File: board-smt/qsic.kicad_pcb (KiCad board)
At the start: 4 copper layers, 214.1 x 131.7 mm, 177 parts, among them Q201 Dual_NMOS, Q202 Dual_NMOS, Q203 Dual_NMOS, Q204 Dual_NMOS, Q205 Dual_NMOS, Q206 Dual_NMOS, Q207 Dual_NMOS, Q208 Dual_NMOS, Q209 Dual_NMOS, Q210 Dual_NMOS, Q211 Dual_NMOS, Q212 Dual_NMOS, Q301 Dual_NMOS, Q302 Dual_NMOS, Q303 Dual_NMOS, Q304 Dual_NMOS, Q305 Dual_NMOS, Q306 Dual_NMOS, Q307 Dual_NMOS, U201 CMP401, U202 CMP401, U203 CMP401, U204 CMP401, U205 CMP401, U206 CMP401, U301 CMP401, U302 CMP401, U303 CMP401, U304 CMP401, U305 CMP401

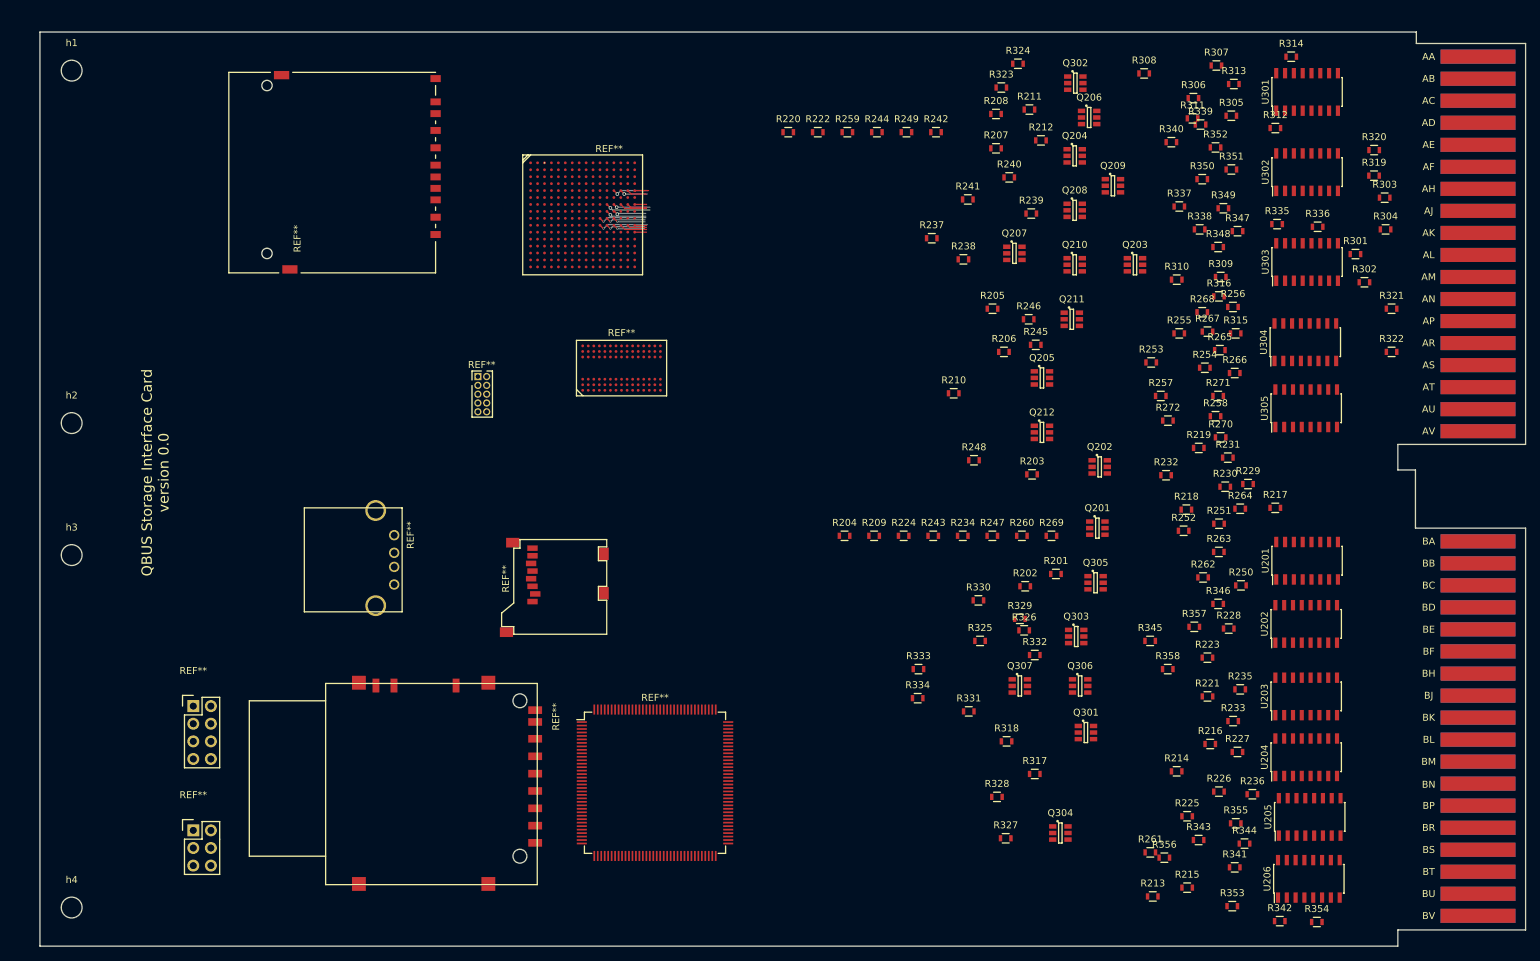
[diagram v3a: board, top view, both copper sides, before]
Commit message: Added the FPGA and rearranged the sheets.
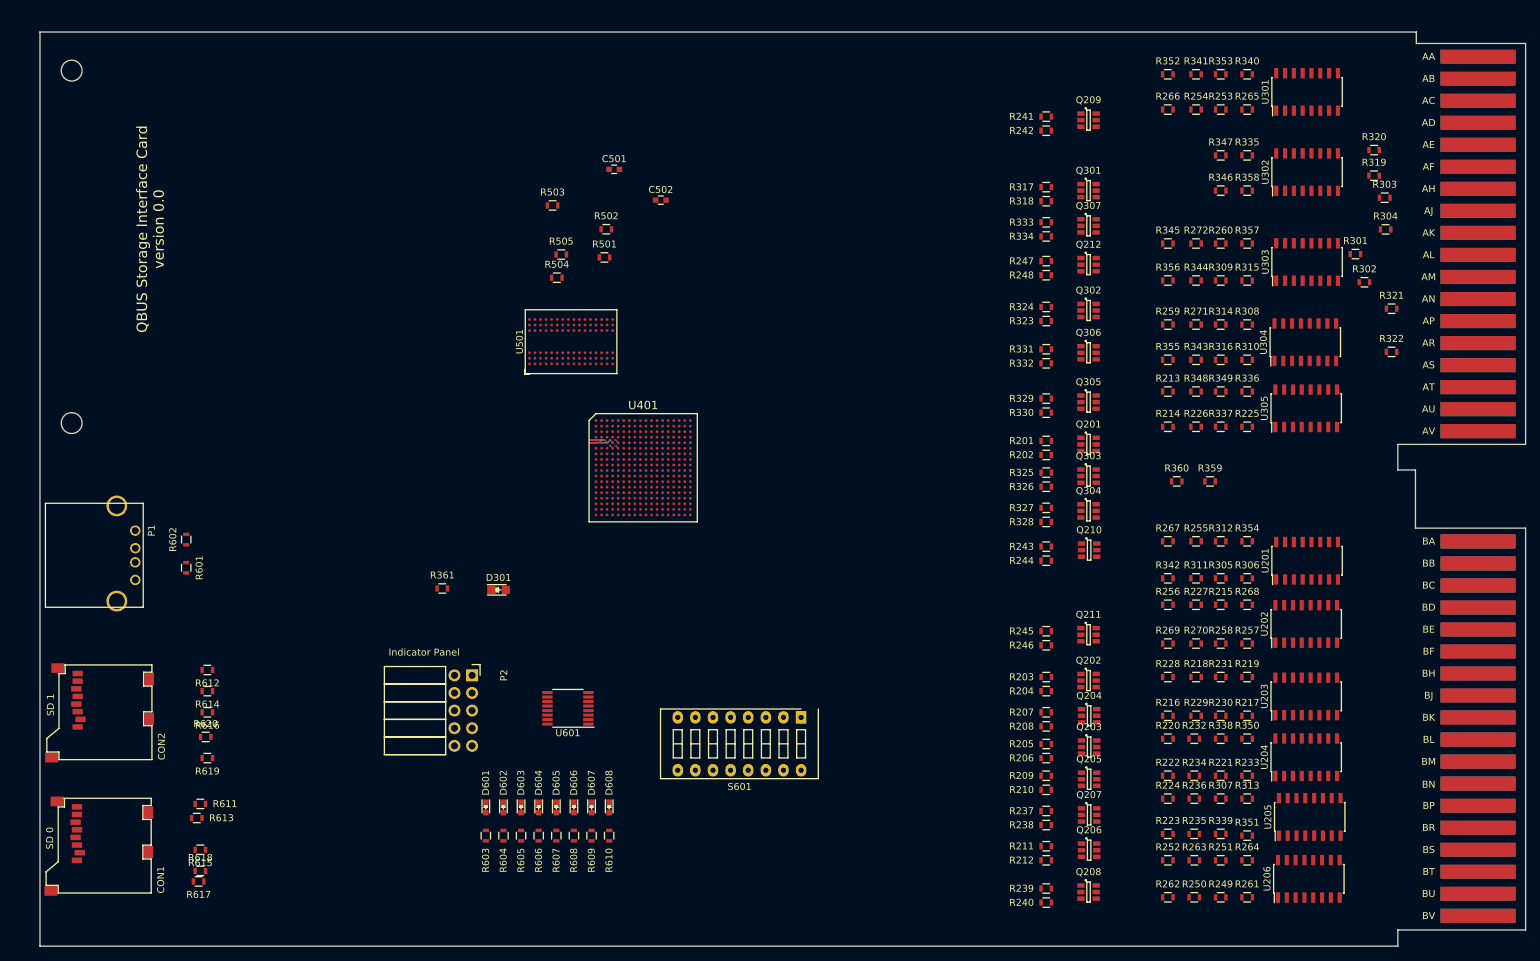
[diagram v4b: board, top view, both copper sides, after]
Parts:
- removed the REF** at (110.5, 51.8)
- removed the REF** at (101.3, 98.3)
- removed the REF** at (32.3, 126.1)
- removed the REF** at (116.1, 73.8)
- removed the REF** at (120.9, 133.6)
- removed the REF** at (83.3, 97.9)
- removed the REF** at (89.3, 45.2)
- removed the REF** at (54.4, 122.6)
- removed the REF** at (54.4, 140.5)
- removed the REF** at (95.4, 75.1)
- removed the REF** at (101.4, 121.8)
- removed h3, h4: MountingHole_3mm, Mounting_Holes:MountingHole_3mm
- added C501: 100nF, Capacitors_SMD:C_0603, F.Cu at (115.0, 45.2)
- added C502: 100nF, Capacitors_SMD:C_0603, F.Cu at (121.7, 49.6)
- added CON1: SD 0, myMods.pretty:microSD-3M-2900-series, F.Cu at (35.7, 135.6)
- added CON2: SD 1, microSD-3M-2900-series, F.Cu at (35.8, 116.4)
- added D301: LED_Small_ALT, LEDs:LED-0805, F.Cu at (98.4, 105.8)
- added D601: LED 0, LEDs:LED-0603, F.Cu at (96.5, 137.2)
- added D602: LED 1, LEDs:LED-0603, F.Cu at (99.1, 137.2)
- added D603: LED 2, LEDs:LED-0603, F.Cu at (101.6, 137.2)
- added D604: LED 3, LEDs:LED-0603, F.Cu at (104.1, 137.2)
- added D605: LED 4, LEDs:LED-0603, F.Cu at (106.7, 137.2)
- added D606: LED 5, LEDs:LED-0603, F.Cu at (109.2, 137.2)
- added D607: LED 6, LEDs:LED-0603, F.Cu at (111.8, 137.2)
- added D608: LED 7, LEDs:LED-0603, F.Cu at (114.3, 137.2)
- added P1: USB_A, Connect:USB_A, F.Cu at (46.0, 97.3)
- added P2: Indicator Panel, Socket_Strips:Socket_Strip_Angled_2x05, F.Cu at (94.5, 118.1)
- added R359: 5kΩ, Resistors_SMD:R_0603, F.Cu at (200.9, 90.2)
- added R360: 5kΩ, Resistors_SMD:R_0603, F.Cu at (196.1, 90.2)
- added R361: 240, Resistors_SMD:R_0603, F.Cu at (90.2, 105.6)
- added R501: 47k, Resistors_SMD:R_0603, F.Cu at (113.6, 57.9)
- added R502: 89, Resistors_SMD:R_0603, F.Cu at (113.9, 53.8)
- added R503: 47, Resistors_SMD:R_0603, F.Cu at (106.1, 50.4)
- added R504: 47, Resistors_SMD:R_0603, F.Cu at (106.8, 60.8)
- added R505: 240, Resistors_SMD:R_0603, F.Cu at (107.4, 57.5)
- added R601: 15k, Resistors_SMD:R_0603, F.Cu at (53.3, 102.6)
- added R602: 15k, Resistors_SMD:R_0603, F.Cu at (53.3, 98.6)
- added R603: R, Resistors_SMD:R_0603, F.Cu at (96.5, 141.2)
- added R604: R, Resistors_SMD:R_0603, F.Cu at (99.1, 141.2)
- added R605: R, Resistors_SMD:R_0603, F.Cu at (101.6, 141.2)
- added R606: R, Resistors_SMD:R_0603, F.Cu at (104.1, 141.2)
- added R607: R, Resistors_SMD:R_0603, F.Cu at (106.7, 141.2)
- added R608: R, Resistors_SMD:R_0603, F.Cu at (109.2, 141.2)
- added R609: R, Resistors_SMD:R_0603, F.Cu at (111.8, 141.2)
- added R610: R, Resistors_SMD:R_0603, F.Cu at (114.3, 141.2)
- added R611: 50k, Resistors_SMD:R_0603, F.Cu at (55.4, 136.7)
- added R612: 50k, Resistors_SMD:R_0603, F.Cu at (56.4, 117.3)
- added R613: 50k, Resistors_SMD:R_0603, F.Cu at (54.9, 138.7)
- added R614: 50k, Resistors_SMD:R_0603, F.Cu at (56.4, 120.4)
- added R615: 50k, Resistors_SMD:R_0603, F.Cu at (55.4, 143.3)
- added R616: 50k, Resistors_SMD:R_0603, F.Cu at (56.4, 123.4)
- added R617: 50k, Resistors_SMD:R_0603, F.Cu at (55.1, 147.8)
- added R618: 270k, Resistors_SMD:R_0603, F.Cu at (55.4, 146.3)
- added R619: 50k, Resistors_SMD:R_0603, F.Cu at (56.4, 130.0)
- added R620: 270k, Resistors_SMD:R_0603, F.Cu at (56.1, 127.0)
- added S601: Config, Buttons_Switches_ThroughHole:SW_DIP_x8_Slide, F.Cu at (142.0, 124.2)
- added U401: XC7A75T-CSG324, myMods.pretty:CSG324, F.Cu at (119.2, 88.2)
- added U501: IS43TR16128B, Housings_BGA:BGA-96_2x3x16_9.0x13.0mm_Pitch0.8mm, F.Cu at (108.8, 70.0)
- added U601: MAX3033E, Housings_SSOP:TSSOP-16_4.4x5mm_Pitch0.65mm, F.Cu at (108.3, 122.9)
- R213, R214, R215, R216, R217, R218, R219, R220, R221, R222, R223, R224, R249, R250, R251, R252, R253, R254, R255, R256, R257, R258, R259, R260, R305, R306, R307, R308, R309, R310, R337, R338, R339, R340, R341, R342, R343, R344, R345, R346: value R -> 20kΩ
- R225, R226, R227, R228, R229, R230, R231, R232, R233, R234, R235, R236, R261, R262, R263, R264, R265, R266, R267, R268, R269, R270, R271, R272, R311, R312, R313, R314, R315, R316, R349, R350, R351, R352, R353, R354, R355, R356, R357, R358: value R -> 340kΩ
- moved R353 119.9 mm to (202.4, 31.5)
- moved R249 119.2 mm to (202.4, 150.1)
- moved R341 114.4 mm to (198.9, 31.5)
- moved R211 106.2 mm to (177.3, 142.7), turned to 180 degrees
- moved R307 105.7 mm to (202.4, 135.9)
- moved Q206 105.6 mm to (183.5, 143.3)
- moved R222 105.6 mm to (194.8, 132.6)
- moved R240 104.7 mm to (177.3, 150.9), turned to 180 degrees
- moved R212 103.8 mm to (177.3, 144.8), turned to 180 degrees
- moved R220 103.1 mm to (194.8, 127.3)
- moved R313 103.0 mm to (206.2, 135.9)
- moved R339 102.3 mm to (202.4, 141.0)
- moved Q208 98.3 mm to (183.4, 149.4)
- moved R239 97.3 mm to (177.3, 148.8), turned to 180 degrees
- moved R351 96.0 mm to (206.2, 141.2)
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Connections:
- net BBS7 renamed /Address/Data/BBS7
- net BDAL0 renamed /BDAL0
- net BDAL1 renamed /BDAL1
- net BDAL10 renamed /BDAL10
- net BDAL11 renamed /BDAL11
- net BDAL12 renamed /BDAL12
- net BDAL13 renamed /BDAL13
- net BDAL14 renamed /BDAL14
- net BDAL15 renamed /BDAL15
- net BDAL16 renamed /BDAL16
- net BDAL17 renamed /BDAL17
- net BDAL18 renamed /BDAL18
- net BDAL19 renamed /BDAL19
- net BDAL2 renamed /BDAL2
- net BDAL20 renamed /BDAL20
- net BDAL21 renamed /BDAL21
- net BDAL3 renamed /BDAL3
- net BDAL4 renamed /BDAL4
- net BDAL5 renamed /BDAL5
- net BDAL6 renamed /BDAL6
- net BDAL7 renamed /BDAL7
- net BDAL8 renamed /BDAL8
- net BDAL9 renamed /BDAL9
- net BDCOK renamed /Bus Control/BDCOK
- net BDMGI renamed /Bus Control/BDMGI
- net BDMGO renamed /Bus Control/BDMGO
- net BEVNT renamed /Bus Control/BEVNT
- net BHALT renamed /Bus Control/BHALT
- net BIAKI renamed /Bus Control/BIAKI
- net BIAKO renamed /Bus Control/BIAKO
- net BPOK renamed /Bus Control/BPOK
- net BSYNC renamed /Bus Control/BSYNC
- net BWTBT renamed /Address/Data/BWTBT
- net RBS7 renamed /RBS7
- net RDAL0 renamed /Address/Data/RDAL0
- net RDAL1 renamed /Address/Data/RDAL1
- net RDAL10 renamed /Address/Data/RDAL10
- net RDAL11 renamed /Address/Data/RDAL11
- net RDAL12 renamed /Address/Data/RDAL12
- net RDAL13 renamed /Address/Data/RDAL13
- net RDAL14 renamed /Address/Data/RDAL14
- net RDAL15 renamed /Address/Data/RDAL15
- net RDAL16 renamed /Address/Data/RDAL16
- net RDAL17 renamed /Address/Data/RDAL17
- net RDAL18 renamed /Address/Data/RDAL18
- net RDAL19 renamed /Address/Data/RDAL19
- net RDAL2 renamed /Address/Data/RDAL2
- net RDAL20 renamed /Address/Data/RDAL20
- net RDAL21 renamed /Address/Data/RDAL21
- net RDAL3 renamed /Address/Data/RDAL3
- net RDAL4 renamed /Address/Data/RDAL4
- net RDAL5 renamed /Address/Data/RDAL5
- net RDAL6 renamed /Address/Data/RDAL6
- net RDAL7 renamed /Address/Data/RDAL7
- net RDAL8 renamed /Address/Data/RDAL8
- net RDAL9 renamed /Address/Data/RDAL9
- net RDCOK renamed /RDCOK
- net RDMGI renamed /RDMGI
- net REVNT renamed /REVNT
- net RHALT renamed /RHALT
- net RIAKI renamed /RIAKI
- net RPOK renamed /RPOK
- net RSYNC renamed /RSYNC
- net RWTBT renamed /RWTBT
- net TBS7 renamed /TBS7
- net TDAL0 renamed /Address/Data/TDAL0
- net TDAL1 renamed /Address/Data/TDAL1
- net TDAL10 renamed /Address/Data/TDAL10
- net TDAL11 renamed /Address/Data/TDAL11
- net TDAL12 renamed /Address/Data/TDAL12
- net TDAL13 renamed /Address/Data/TDAL13
- net TDAL14 renamed /Address/Data/TDAL14
- net TDAL15 renamed /Address/Data/TDAL15
- net TDAL16 renamed /Address/Data/TDAL16
- net TDAL17 renamed /Address/Data/TDAL17
- net TDAL18 renamed /Address/Data/TDAL18
- net TDAL19 renamed /Address/Data/TDAL19
- net TDAL2 renamed /Address/Data/TDAL2
- net TDAL20 renamed /Address/Data/TDAL20
- net TDAL21 renamed /Address/Data/TDAL21
- net TDAL3 renamed /Address/Data/TDAL3
- net TDAL4 renamed /Address/Data/TDAL4
- net TDAL5 renamed /Address/Data/TDAL5
- net TDAL6 renamed /Address/Data/TDAL6
- net TDAL7 renamed /Address/Data/TDAL7
- net TDAL8 renamed /Address/Data/TDAL8
- net TDAL9 renamed /Address/Data/TDAL9
- net TDIN renamed /TDIN
- net TDMGO renamed /TDMGO
- net TDMR renamed /TDMR
- net TDOUT renamed /TDOUT
- net TIAKO renamed /TIAKO
- net TINIT renamed /TINIT
- net TIRQ4 renamed /TIRQ4
- net TIRQ5 renamed /TIRQ5
- net TIRQ6 renamed /TIRQ6
- net TIRQ7 renamed /TIRQ7
- net TREF renamed /TREF
- net TRPLY renamed /TRPLY
- net TSACK renamed /TSACK
- net TSYNC renamed /TSYNC
- net TWTBT renamed /TWTBT
- B101 pad AA1: BIRQ5 -> /Bus Control/BIRQ5
- B101 pad AB1: BIRQ6 -> /Bus Control/BIRQ6
- B101 pad AE2: BDOUT -> /Bus Control/BDOUT
- B101 pad AF2: BRPLY -> /Bus Control/BRPLY
- B101 pad AH2: BDIN -> /Bus Control/BDIN
- B101 pad AL2: BIRQ4 -> /Bus Control/BIRQ4
- B101 pad AN1: BDMR -> /Bus Control/BDMR
- B101 pad AR1: BREF -> /Bus Control/BREF
- B101 pad AT2: BINIT -> /Bus Control/BINIT
- B101 pad BN1: BSACK -> /Bus Control/BSACK
- B101 pad BP1: BIRQ7 -> /Bus Control/BIRQ7
- Q302 pad 3: BDIN -> /Bus Control/BDIN
- Q303 pad 3: BRPLY -> /Bus Control/BRPLY
- Q303 pad 6: BDOUT -> /Bus Control/BDOUT
- Q304 pad 3: BINIT -> /Bus Control/BINIT
- Q304 pad 6: BREF -> /Bus Control/BREF
- Q305 pad 3: BSACK -> /Bus Control/BSACK
- Q305 pad 6: BDMR -> /Bus Control/BDMR
- Q306 pad 3: BIRQ5 -> /Bus Control/BIRQ5
- Q306 pad 6: BIRQ4 -> /Bus Control/BIRQ4
- Q307 pad 3: BIRQ7 -> /Bus Control/BIRQ7
- Q307 pad 6: BIRQ6 -> /Bus Control/BIRQ6
- R213 pad 1: +1V5 -> Net-(R213-Pad1)
- R213 pad 2: Net-(R213-Pad2) -> +1V5
- R214 pad 1: +1V5 -> Net-(R214-Pad1)
- R214 pad 2: Net-(R214-Pad2) -> +1V5
- R215 pad 1: +1V5 -> Net-(R215-Pad1)
- R215 pad 2: Net-(R215-Pad2) -> +1V5
- R216 pad 1: +1V5 -> Net-(R216-Pad1)
- R216 pad 2: Net-(R216-Pad2) -> +1V5
- R217 pad 1: +1V5 -> Net-(R217-Pad1)
- R217 pad 2: Net-(R217-Pad2) -> +1V5
- R218 pad 1: +1V5 -> Net-(R218-Pad1)
- R218 pad 2: Net-(R218-Pad2) -> +1V5
- R219 pad 1: +1V5 -> Net-(R219-Pad1)
- R219 pad 2: Net-(R219-Pad2) -> +1V5
- R220 pad 1: +1V5 -> Net-(R220-Pad1)
- R220 pad 2: Net-(R220-Pad2) -> +1V5
- R221 pad 1: +1V5 -> Net-(R221-Pad1)
- R221 pad 2: Net-(R221-Pad2) -> +1V5
- R222 pad 1: +1V5 -> Net-(R222-Pad1)
- R222 pad 2: Net-(R222-Pad2) -> +1V5
- R223 pad 1: +1V5 -> Net-(R223-Pad1)
- R223 pad 2: Net-(R223-Pad2) -> +1V5
- R224 pad 1: +1V5 -> Net-(R224-Pad1)
- R224 pad 2: Net-(R224-Pad2) -> +1V5
- R225 pad 1: Net-(R213-Pad2) -> Net-(R213-Pad1)
- R226 pad 1: Net-(R214-Pad2) -> Net-(R214-Pad1)
- R227 pad 1: Net-(R215-Pad2) -> Net-(R215-Pad1)
- R228 pad 1: Net-(R216-Pad2) -> Net-(R216-Pad1)
- R229 pad 1: Net-(R217-Pad2) -> Net-(R217-Pad1)
- R230 pad 1: Net-(R218-Pad2) -> Net-(R218-Pad1)
- R231 pad 1: Net-(R219-Pad2) -> Net-(R219-Pad1)
- R232 pad 1: Net-(R220-Pad2) -> Net-(R220-Pad1)
- R233 pad 1: Net-(R221-Pad2) -> Net-(R221-Pad1)
- R234 pad 1: Net-(R222-Pad2) -> Net-(R222-Pad1)
- R235 pad 1: Net-(R223-Pad2) -> Net-(R223-Pad1)
- R236 pad 1: Net-(R224-Pad2) -> Net-(R224-Pad1)
- R249 pad 1: +1V5 -> Net-(R249-Pad1)
- R249 pad 2: Net-(R249-Pad2) -> +1V5
- R250 pad 1: +1V5 -> Net-(R250-Pad1)
- R250 pad 2: Net-(R250-Pad2) -> +1V5
- R251 pad 1: +1V5 -> Net-(R251-Pad1)
- R251 pad 2: Net-(R251-Pad2) -> +1V5
- R252 pad 1: +1V5 -> Net-(R252-Pad1)
- R252 pad 2: Net-(R252-Pad2) -> +1V5
- R253 pad 1: +1V5 -> Net-(R253-Pad1)
- R253 pad 2: Net-(R253-Pad2) -> +1V5
- R254 pad 1: +1V5 -> Net-(R254-Pad1)
- R254 pad 2: Net-(R254-Pad2) -> +1V5
- R255 pad 1: +1V5 -> Net-(R255-Pad1)
- R255 pad 2: Net-(R255-Pad2) -> +1V5
- R256 pad 1: +1V5 -> Net-(R256-Pad1)
- R256 pad 2: Net-(R256-Pad2) -> +1V5
- R257 pad 1: +1V5 -> Net-(R257-Pad1)
- R257 pad 2: Net-(R257-Pad2) -> +1V5
- R258 pad 1: +1V5 -> Net-(R258-Pad1)
- R258 pad 2: Net-(R258-Pad2) -> +1V5
- R259 pad 1: +1V5 -> Net-(R259-Pad1)
- R259 pad 2: Net-(R259-Pad2) -> +1V5
- R260 pad 1: +1V5 -> Net-(R260-Pad1)
- R260 pad 2: Net-(R260-Pad2) -> +1V5
- R261 pad 1: Net-(R249-Pad2) -> Net-(R249-Pad1)
- R262 pad 1: Net-(R250-Pad2) -> Net-(R250-Pad1)
- R263 pad 1: Net-(R251-Pad2) -> Net-(R251-Pad1)
- R264 pad 1: Net-(R252-Pad2) -> Net-(R252-Pad1)
- R265 pad 1: Net-(R253-Pad2) -> Net-(R253-Pad1)
- R266 pad 1: Net-(R254-Pad2) -> Net-(R254-Pad1)
- R267 pad 1: Net-(R255-Pad2) -> Net-(R255-Pad1)
- R268 pad 1: Net-(R256-Pad2) -> Net-(R256-Pad1)
- R269 pad 1: Net-(R257-Pad2) -> Net-(R257-Pad1)
- R270 pad 1: Net-(R258-Pad2) -> Net-(R258-Pad1)
- R271 pad 1: Net-(R259-Pad2) -> Net-(R259-Pad1)
- R272 pad 1: Net-(R260-Pad2) -> Net-(R260-Pad1)
- R335 pad 1: +1V5 -> Net-(R335-Pad1)
- R335 pad 2: Net-(R335-Pad2) -> +1V5
- R336 pad 1: +1V5 -> Net-(R336-Pad1)
- R336 pad 2: Net-(R336-Pad2) -> +1V5
- R337 pad 1: +1V5 -> Net-(R337-Pad1)
- R337 pad 2: Net-(R337-Pad2) -> +1V5
- R338 pad 1: +1V5 -> Net-(R338-Pad1)
- R338 pad 2: Net-(R338-Pad2) -> +1V5
- R339 pad 1: +1V5 -> Net-(R339-Pad1)
- R339 pad 2: Net-(R339-Pad2) -> +1V5
- R340 pad 1: +1V5 -> Net-(R340-Pad1)
- R340 pad 2: Net-(R340-Pad2) -> +1V5
- R341 pad 1: +1V5 -> Net-(R341-Pad1)
- R341 pad 2: Net-(R341-Pad2) -> +1V5
- R342 pad 1: +1V5 -> Net-(R342-Pad1)
- R342 pad 2: Net-(R342-Pad2) -> +1V5
- R343 pad 1: +1V5 -> Net-(R343-Pad1)
- R343 pad 2: Net-(R343-Pad2) -> +1V5
- R344 pad 1: +1V5 -> Net-(R344-Pad1)
- R344 pad 2: Net-(R344-Pad2) -> +1V5
- R345 pad 1: +1V5 -> Net-(R345-Pad1)
- R345 pad 2: Net-(R345-Pad2) -> +1V5
- R346 pad 1: +1V5 -> Net-(R346-Pad1)
- R346 pad 2: Net-(R346-Pad2) -> +1V5
- R347 pad 1: Net-(R335-Pad2) -> Net-(R335-Pad1)
- R348 pad 1: Net-(R336-Pad2) -> Net-(R336-Pad1)
- R348 pad 2: RDIN -> /RDIN
- R349 pad 1: Net-(R337-Pad2) -> Net-(R337-Pad1)
- R349 pad 2: RDOUT -> /RDOUT
- R350 pad 1: Net-(R338-Pad2) -> Net-(R338-Pad1)
- R350 pad 2: RRPLY -> /RRPLY
- R351 pad 1: Net-(R339-Pad2) -> Net-(R339-Pad1)
- R351 pad 2: RREF -> /RREF
- R352 pad 1: Net-(R340-Pad2) -> Net-(R340-Pad1)
- R352 pad 2: RINIT -> /RINIT
- R353 pad 1: Net-(R341-Pad2) -> Net-(R341-Pad1)
- R353 pad 2: RDMR -> /RDMR
- R354 pad 1: Net-(R342-Pad2) -> Net-(R342-Pad1)
- R354 pad 2: RSACK -> /RSACK
- R355 pad 1: Net-(R343-Pad2) -> Net-(R343-Pad1)
- R355 pad 2: RIRQ4 -> /RIRQ4
- R356 pad 1: Net-(R344-Pad2) -> Net-(R344-Pad1)
- R356 pad 2: RIRQ5 -> /RIRQ5
- R357 pad 1: Net-(R345-Pad2) -> Net-(R345-Pad1)
- R357 pad 2: RIRQ6 -> /RIRQ6
- R358 pad 1: Net-(R346-Pad2) -> Net-(R346-Pad1)
- R358 pad 2: RIRQ7 -> /RIRQ7
- U201 pad 11: (no net) -> Net-(R342-Pad1)
- U201 pad 12: (no net) -> /Bus Control/BSACK
- U201 pad 15: (no net) -> /RSACK
- U201 pad 9: Net-(R255-Pad2) -> Net-(R255-Pad1)
- U202 pad 11: Net-(R256-Pad2) -> Net-(R256-Pad1)
- U202 pad 6: Net-(R257-Pad2) -> Net-(R257-Pad1)
- U202 pad 8: Net-(R258-Pad2) -> Net-(R258-Pad1)
- U202 pad 9: Net-(R215-Pad2) -> Net-(R215-Pad1)
- U203 pad 11: Net-(R216-Pad2) -> Net-(R216-Pad1)
- U203 pad 6: Net-(R217-Pad2) -> Net-(R217-Pad1)
- U203 pad 8: Net-(R218-Pad2) -> Net-(R218-Pad1)
- U203 pad 9: Net-(R219-Pad2) -> Net-(R219-Pad1)
- U204 pad 10: BSACK -> /Bus Control/BRPLY
- U204 pad 11: Net-(R220-Pad2) -> Net-(R220-Pad1)
- U204 pad 16: RSACK -> /RRPLY
- U204 pad 6: Net-(R221-Pad2) -> Net-(R221-Pad1)
- U204 pad 8: Net-(R222-Pad2) -> Net-(R222-Pad1)
- U204 pad 9: Net-(R342-Pad2) -> Net-(R338-Pad1)
- U205 pad 1: RIRQ7 -> /RREF
- U205 pad 11: Net-(R224-Pad2) -> Net-(R224-Pad1)
- U205 pad 6: Net-(R223-Pad2) -> Net-(R223-Pad1)
- U205 pad 7: BIRQ7 -> /Bus Control/BREF
- U205 pad 8: Net-(R346-Pad2) -> Net-(R339-Pad1)
- U206 pad 11: Net-(R252-Pad2) -> Net-(R252-Pad1)
- U206 pad 6: Net-(R249-Pad2) -> Net-(R249-Pad1)
- U206 pad 8: Net-(R250-Pad2) -> Net-(R250-Pad1)
- U206 pad 9: Net-(R251-Pad2) -> Net-(R251-Pad1)
- U301 pad 10: BIRQ6 -> /Bus Control/BINIT
- U301 pad 11: Net-(R344-Pad2) -> Net-(R341-Pad1)
- U301 pad 12: BIRQ5 -> /Bus Control/BDMR
- U301 pad 15: RIRQ5 -> /RDMR
- U301 pad 16: RIRQ6 -> /RINIT
- U301 pad 6: Net-(R253-Pad2) -> Net-(R253-Pad1)
- U301 pad 8: Net-(R254-Pad2) -> Net-(R254-Pad1)
- U301 pad 9: Net-(R345-Pad2) -> Net-(R340-Pad1)
- U302 pad 1: RRPLY -> (no net)
- U302 pad 11: Net-(R336-Pad2) -> (no net)
- U302 pad 12: BDIN -> (no net)
- U302 pad 15: RDIN -> (no net)
- U302 pad 2: RDOUT -> /RIRQ7
- U302 pad 5: BDOUT -> /Bus Control/BIRQ7
- U302 pad 6: Net-(R337-Pad2) -> Net-(R346-Pad1)
- U302 pad 7: BRPLY -> (no net)
- U302 pad 8: Net-(R338-Pad2) -> (no net)
- U302 pad 9: Net-(R335-Pad2) -> Net-(R335-Pad1)
- U303 pad 10: BIRQ4 -> /Bus Control/BIRQ6
- U303 pad 11: Net-(R260-Pad2) -> Net-(R260-Pad1)
- U303 pad 16: RIRQ4 -> /RIRQ6
- U303 pad 2: RDMR -> /RIRQ5
- U303 pad 5: BDMR -> /Bus Control/BIRQ5
- U303 pad 6: Net-(R341-Pad2) -> Net-(R344-Pad1)
- U303 pad 9: Net-(R343-Pad2) -> Net-(R345-Pad1)
- U304 pad 2: RREF -> /RIRQ4
- U304 pad 5: BREF -> /Bus Control/BIRQ4
- U304 pad 6: Net-(R339-Pad2) -> Net-(R343-Pad1)
- U304 pad 9: Net-(R259-Pad2) -> Net-(R259-Pad1)
- U305 pad 10: (no net) -> /Bus Control/BDIN
- U305 pad 11: Net-(R340-Pad2) -> Net-(R337-Pad1)
- U305 pad 12: BINIT -> /Bus Control/BDOUT
- U305 pad 15: RINIT -> /RDOUT
- U305 pad 16: (no net) -> /RDIN
- U305 pad 6: Net-(R213-Pad2) -> Net-(R213-Pad1)
- U305 pad 8: Net-(R214-Pad2) -> Net-(R214-Pad1)
- U305 pad 9: (no net) -> Net-(R336-Pad1)
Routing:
- net (no net): track 90.7 -> 0.00 mm, vias 12 -> 0
- net /Memory/BA0: track 0.00 -> 4.21 mm, vias 0 -> 1
- net /Memory/DQL4: track 0.00 -> 3.61 mm, vias 0 -> 1
- net GND: track 0.00 -> 3.53 mm, vias 0 -> 1
- net /Memory/RAS#: track 0.00 -> 2.57 mm, vias 0 -> 1
- net /Memory/DQL2: track 0.00 -> 1.97 mm
- net /Memory/DQL3: track 0.00 -> 1.00 mm
- net /Memory/ODT: track 0.00 -> 0.57 mm, vias 0 -> 1
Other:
- net class Default: clearance 0.2032 -> 0.127
- rule trace_clearance: 0.2032 -> 0.127

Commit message: Added some voltage regulators.
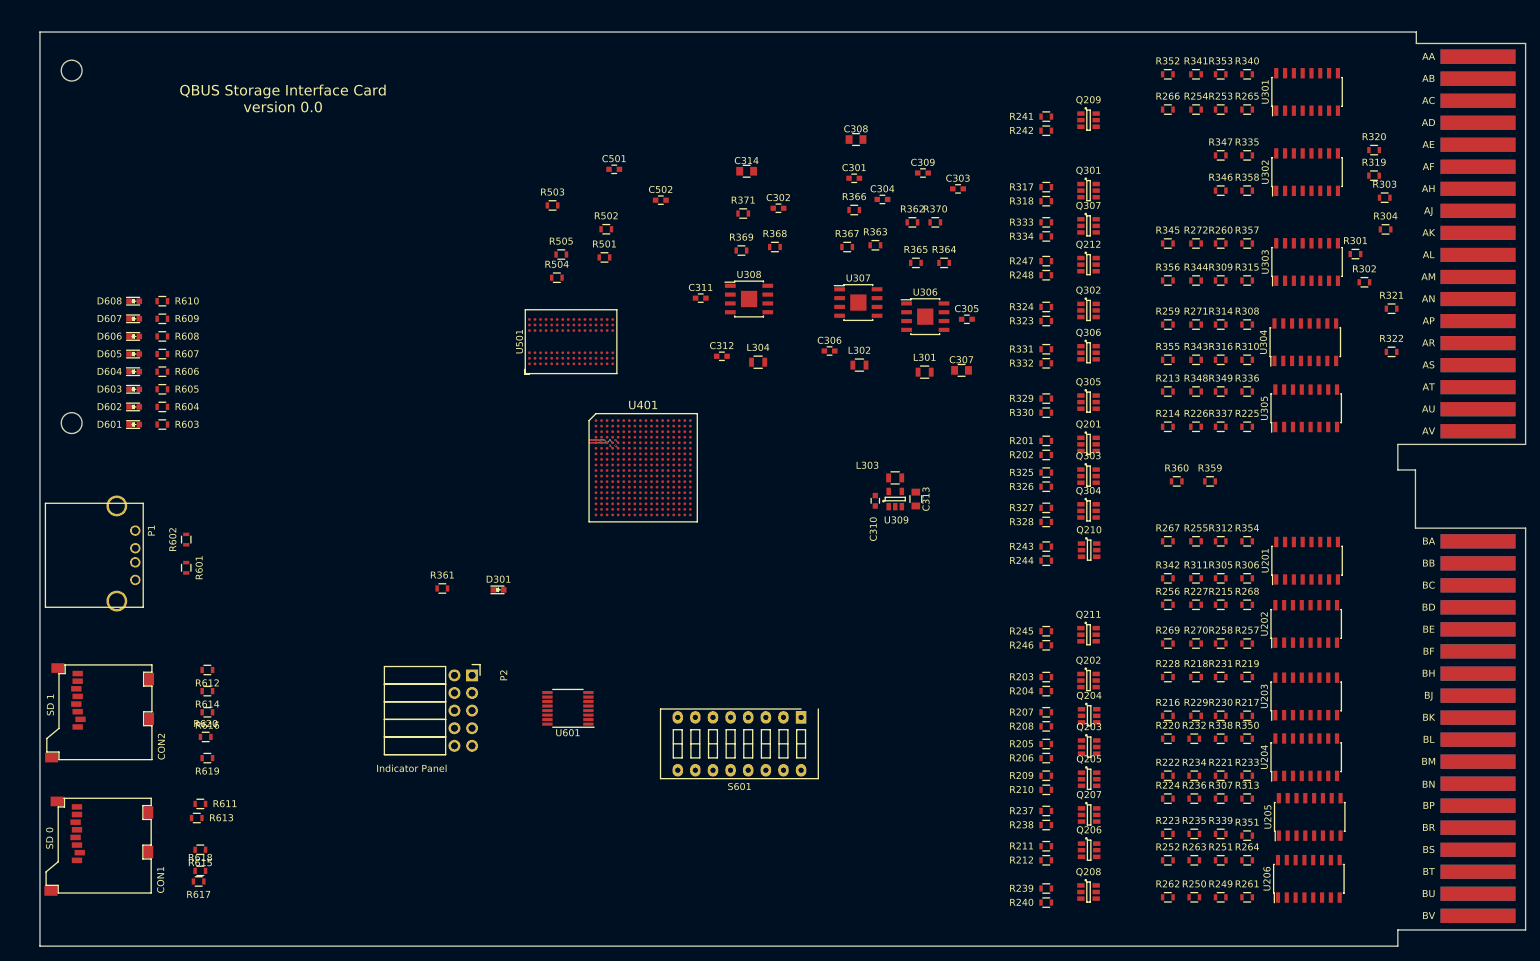
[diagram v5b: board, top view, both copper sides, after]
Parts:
- added C301: 10uF, Capacitors_SMD:C_0603, F.Cu at (149.6, 46.5)
- added C302: 10uF, Capacitors_SMD:C_0603, F.Cu at (138.7, 50.8)
- added C303: 2.2nF, Capacitors_SMD:C_0603, F.Cu at (164.6, 48.0)
- added C304: 2.2nF, Capacitors_SMD:C_0603, F.Cu at (153.7, 49.5)
- added C305: 100nF, Capacitors_SMD:C_0603, F.Cu at (165.8, 66.8)
- added C306: 100nF, Capacitors_SMD:C_0603, F.Cu at (146.1, 71.4)
- added C307: 22uF, Capacitors_SMD:C_0805, F.Cu at (165.1, 74.2)
- added C308: 22uF, Capacitors_SMD:C_0805, F.Cu at (149.9, 40.9)
- added C309: 10uF, Capacitors_SMD:C_0603, F.Cu at (159.5, 45.7)
- added C310: 10uF, Capacitors_SMD:C_0603, F.Cu at (152.7, 93.0)
- added C311: 100nF, Capacitors_SMD:C_0603, F.Cu at (127.5, 63.8)
- added C312: 100nF, Capacitors_SMD:C_0603, F.Cu at (130.5, 72.1)
- added C313: 22uF, Capacitors_SMD:C_0805, F.Cu at (158.5, 92.7)
- added C314: 22uF, Capacitors_SMD:C_0805, F.Cu at (134.1, 45.5)
- added L301: 4.7uH, Resistors_SMD:R_0805, F.Cu at (159.8, 74.4)
- added L302: 4.7uH, Resistors_SMD:R_0805, F.Cu at (150.4, 73.4)
- added L303: 1.5uH, Resistors_SMD:R_0805, F.Cu at (155.5, 89.7)
- added L304: 2.2uH, Resistors_SMD:R_0805, F.Cu at (135.8, 73.0)
- added R362: 7.5k, Resistors_SMD:R_0603, F.Cu at (158.0, 52.8)
- added R363: 7.5k, Resistors_SMD:R_0603, F.Cu at (152.7, 56.1)
- added R364: 31.1k, Resistors_SMD:R_0603, F.Cu at (162.6, 58.7)
- added R365: 10k, Resistors_SMD:R_0603, F.Cu at (158.5, 58.7)
- added R366: 10k, Resistors_SMD:R_0603, F.Cu at (149.6, 51.1)
- added R367: 11.5k, Resistors_SMD:R_0603, F.Cu at (148.6, 56.4)
- added R368: 100k, Resistors_SMD:R_0603, F.Cu at (138.2, 56.4)
- added R369: 50k, Resistors_SMD:R_0603, F.Cu at (133.4, 56.9)
- added R370: 18.2k, Resistors_SMD:R_0603, F.Cu at (161.3, 52.8)
- added R371: 4.7k, Resistors_SMD:R_0603, F.Cu at (133.6, 51.6)
- added U306: AOZ3010PI, Housings_SOIC:SOIC-8-1EP_3.9x4.9mm_Pitch1.27mm, F.Cu at (159.9, 66.4)
- added U307: AOZ3010PI, Housings_SOIC:SOIC-8-1EP_3.9x4.9mm_Pitch1.27mm, F.Cu at (150.2, 64.4)
- added U308: RT8288A, Housings_SOIC:SOIC-8-1EP_3.9x4.9mm_Pitch1.27mm, F.Cu at (134.5, 63.9)
- added U309: SC189, TO_SOT_Packages_SMD:SOT-23-5, F.Cu at (155.5, 92.7)
- CON2: footprint microSD-3M-2900-series -> myMods.pretty:microSD-3M-2900-series
- D301: footprint LEDs:LED-0805 -> LEDs:LED-0603
- moved R610 100.4 mm to (49.9, 64.2), turned to 180 degrees
- moved D608 100.1 mm to (45.8, 64.2), turned to 0 degrees
- moved R609 96.8 mm to (49.9, 66.7), turned to 180 degrees
- moved D607 96.5 mm to (45.8, 66.7), turned to 0 degrees
- moved R608 93.3 mm to (49.9, 69.3), turned to 180 degrees
- moved D606 92.9 mm to (45.8, 69.3), turned to 0 degrees
- moved R607 89.7 mm to (49.9, 71.8), turned to 180 degrees
- moved D605 89.3 mm to (45.8, 71.8), turned to 0 degrees
- moved R606 86.1 mm to (49.9, 74.4), turned to 180 degrees
- moved D604 85.7 mm to (45.8, 74.4), turned to 0 degrees
- moved R605 82.5 mm to (49.9, 76.9), turned to 180 degrees
- moved D603 82.1 mm to (45.8, 76.9), turned to 0 degrees
- moved R604 79.0 mm to (49.9, 79.4), turned to 180 degrees
- moved D602 78.5 mm to (45.8, 79.4), turned to 0 degrees
- moved R603 75.4 mm to (49.9, 82.0), turned to 180 degrees
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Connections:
- CON1 pad 9: (no net) -> GND
- CON2 pad 9: (no net) -> GND
